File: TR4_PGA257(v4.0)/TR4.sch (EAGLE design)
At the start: 159 parts, among them IC1 SN74AVC4T774PWR, IC2 W25Q256JVFIQ, IC3 SN74AVC4T774PWR, IC4 SN74AVC4T774PWR, IC6 CP2102-GMR, IC7 LM1117MP-1.8_NOPB, IC8 LM1117MP-1.8_NOPB, IC9 LM1117MP-1.8_NOPB, J1 U-F-M5DD-Y-L, J3 TF-15X15, J4 2985-6004, J5 2985-6004, Q1 FMMT497TA, Q10 BSH103,235, Q11 BSH103,235, Q12 BSH103,235, Q13 BSH103,235, Q2 FMMT497TA, Q3 BSH103,235, Q4 BSH103,235, Q5 BSH103,235, Q6 BSH103,235, Q7 BSH103,235, Q8 BSH103,235, Q9 BSH103,235

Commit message: Add pull resistor for mosfet
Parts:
- added R61, R62, R63, R64, R65, R66, R67, R68, R69, R70, R71: 10k, SparkFun-Resistors:10KOHM-0603-1/10W-1%
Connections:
- net GND: now also R61.1, R62.1, R63.1, R64.1, R65.1, R66.1, R67.1, R68.1, R69.1, R70.1, R71.1
- net LED_0: now also R64.2
- net LED_1: now also R65.2
- net LED_2: now also R66.2
- net LED_3: now also R67.2
- net LED_4: now also R68.2
- net LED_5: now also R69.2
- net LED_6: now also R70.2
- net LED_7: now also R71.2
- net VDD_1.8_1: now also R63.2
- net VDD_1.8_2: now also R61.2
- net VDD_1.8_3: now also R62.2

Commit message: Update signal name and connect pin 59 and 60
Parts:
- removed C1, C10, C11, C6: 0.1uF, SparkFun-Capacitors:0.1UF-0603-25V-5%
- removed C12: 4.7uF, SparkFun-Capacitors:4.7UF0603
- removed C9: 1.0uF, SparkFun-Capacitors:1.0UF-0603-16V-10%
- removed CHILDCLOCK, CLOCK: (no value), pinhead:PINHD-2X2
- removed D1, D2, D3: (no value), SparkFun-LED:LED0603
- removed IC2: W25Q256JVFIQ, SamacSys_Parts:W25Q256JVFIQ
- removed IC6: CP2102-GMR, SamacSys_Parts:CP2102-GMR
- removed J1: U-F-M5DD-Y-L, SamacSys_Parts:U-F-M5DD-Y-L
- removed J2: (no value), SparkFun-Connectors:CONN_07
- removed J3: TF-15X15, SamacSys_Parts:TF-15X15
- removed JP7: PINHD-2X2, Connector:PINHD-2X2
- removed Q1, Q2: FMMT497TA, SamacSys_Parts:FMMT497TA
- removed R11, R12, R13: 10k, SparkFun-Resistors:10KOHM-0603-1/10W-1%
- removed R14, R15, R16, R18, R19, R20, R21: 33, SparkFun-Resistors:33OHM-0603-1/10W-1%
- removed R34, R35, R36, R40, R41, R43, R44: 4.7k, SparkFun-Resistors:4.7KOHM-0603-1/10W-1%
- removed R37, R38, R39: 330, SparkFun-Resistors:330OHM-0603-1/10W-1%
- removed R42, R45: 47k, SparkFun-Resistors:47KOHM-0603-1/10W-1%
- removed R7, R8: 20k, SparkFun-Resistors:20KOHM-0603-1/10W-1%
- added FLASH, SD_CARD: PINHD-2X6, Connector:PINHD-2X6
- added USB-UART: PINHD-2X4, Connector:PINHD-2X4
- C14, C16, C18: value 10uF -> 100uF
- IC7, IC8, IC9: value LM1117MP-1.8_NOPB -> LM1117IMPX-ADJ/NOPB
- R1: value 200 -> 15k; device SparkFun-Resistors:200OHM-0603-1/10W-1% -> SparkFun-Resistors:15KOHM-0603-1/10W-1%
- R2, R4, R6: value 20k -> 6.8k; device SparkFun-Resistors:20KOHM-0603-1/10W-1% -> SparkFun-Resistors:6.8KOHM-0603-1/10W-1%
- R3, R5: value 20k -> 15k; device SparkFun-Resistors:20KOHM-0603-1/10W-1% -> SparkFun-Resistors:15KOHM-0603-1/10W-1%
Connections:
- net VDD_CORE renamed VDD_CHIP
- net VDD_IO_CORE renamed VDD_CHIP_IO
- removed net CD1: R1.2, R8.1
- removed net D+: IC6.D+, J1.3
- removed net D-: IC6.D-, J1.2
- removed net DAT1: J3.DAT1
- removed net DAT2: J3.DAT2, R7.1
- removed net FLASH_HOLD: IC2.!RESET(IO3), R12.1, R18.1
- removed net FLASH_RESET: IC2.!RESET, R13.1, R16.1
- removed net FLASH_WP: IC2.!WP(IO2), R11.1, R21.1
- removed net N$1: J2.4, R14.2
- removed net N$11: J2.7, R21.2
- removed net N$2: J2.5, R19.2
- removed net N$25: IC6.!RST, R34.2
- removed net N$27: IC6.!SUSPEND, R35.2
- removed net N$29: IC6.SUSPEND, R36.2
- removed net N$3: J3.CARD_DETECT, R1.1
- removed net N$30: JP7.2, Q1.C, R40.1
- removed net N$31: Q1.B, R41.1
- removed net N$32: D1.A, R37.1
- removed net N$33: D2.A, R38.1
- removed net N$34: D3.A, R39.1
- removed net N$35: JP7.4, Q2.E, R44.2
- removed net N$36: R43.1, R44.1
- removed net N$37: Q2.B, R43.2
- removed net N$5: J2.3, R15.2
- removed net N$6: J2.6, R20.2
- removed net N$7: J2.1, R18.2
- removed net N$8: J2.2, R16.2
- removed net RXD: D3.C, IC6.RXD, Q2.C, R45.2
- removed net SMA_ICHILD: CHILDCLOCK.1, J5.5
- removed net SMA_ICLK: CLOCK.1, J4.5
- removed net TXD: D2.C, IC6.TXD, Q1.E, R42.1
- removed net VDD_5V: C10.1, C9.1, IC6.REGIN, IC6.VBUS, J1.1, R34.1, R35.1, R37.2
- removed net VDD_CP2102: C11.1, C12.1, IC6.VDD, R38.2, R39.2, R42.2, R45.1
- removed net VDD_IO: C3.1, C5.1, C8.1, IC1.DIR1, IC1.DIR2, IC1.DIR3, IC1.VCCA, IC3.DIR1, IC3.DIR2, IC3.DIR4, IC3.VCCA, IC4.DIR4, IC4.VCCA, JP8.2, R26.2, R27.2, R28.2, R29.2, R30.2, R31.2, R32.2, R33.2, R40.2, R41.2, R58.2, R59.2, R60.2
- new net VDD_1V8: C3.1, C5.1, C8.1, IC1.DIR1, IC1.DIR2, IC1.DIR3, IC1.VCCA, IC3.DIR1, IC3.DIR3, IC3.DIR4, IC3.VCCA, IC4.DIR4, IC4.VCCA, JP8.2, R26.2, R27.2, R28.2, R29.2, R30.2, R31.2, R32.2, R33.2, R58.2, R59.2, R60.2, USB-UART.5
- net B1: now also SD_CARD.12; no longer J3.CD/DAT3, R2.1
- net B2: now also SD_CARD.10; no longer J3.CMD, R3.1
- net B3: now also SD_CARD.6; no longer J3.CLX, R4.1
- net B4: now also SD_CARD.8; no longer J3.DAT0, R5.1
- net CHILDCLOCK: now also J5.5; no longer CHILDCLOCK.2, CHILDCLOCK.4
- net CHILDCLOCK_GPIO: no longer CHILDCLOCK.3
- net CLOCK_GPIO: no longer CLOCK.3
- net CS: now also IC3.A1, JP2.2; no longer IC3.A4, JP2.8
- net DAT0: no longer R6.1
- net FLASH_CS: now also FLASH.12, IC3.B1; no longer IC2.DO(IO1), IC3.B4, R15.1
- net FLASH_MISO: now also FLASH.8, IC3.B2; no longer IC2.!CS, IC3.B3, R14.1
- net FLASH_MOSI: now also FLASH.10, IC3.B3; no longer IC2.DI(IO0), IC3.B2, R19.1
- net FLASH_SCK: now also FLASH.6, IC3.B4; no longer IC2.CLK, IC3.B1, R20.1
- net GND: now also FLASH.3, FLASH.4, IC3.DIR2, R1.1, R2.1, R2.2, R3.1, R4.1, R4.2, R5.1, R6.1, R6.2, SD_CARD.3, SD_CARD.4, USB-UART.1; no longer C1.2, C10.2, C11.2, C12.2, C6.2, C9.2, D1.C, IC2.GND, IC3.DIR3, IC6.GND, J1.10, J1.5, J1.7, J1.8, J1.9, J3.MP1, J3.MP2, J3.MP3, J3.MP4, J3.VSS, R36.1
- net MISO: now also IC3.A2, JP2.4; no longer IC3.A3, JP2.6
- net MOSI: now also IC3.A3, JP2.6; no longer IC3.A2, JP2.4
- net QSPI_CS: now also JP2.1; no longer JP2.7
- net QSPI_MISO: now also JP2.3; no longer JP2.5
- net QSPI_MOSI: now also JP2.5; no longer JP2.3
- net QSPI_SCK: now also JP2.7; no longer JP2.1
- net SCK: now also IC3.A4, JP2.8; no longer IC3.A1, JP2.2
- net SYS_CLK: now also J4.5; no longer CLOCK.2, CLOCK.4
- net TLPORT_A_BITS_PARAM[0]: now also SOCKET_2.28
- net UART_RXD: now also USB-UART.3; no longer JP7.1
- net UART_TXD: now also USB-UART.7; no longer JP7.3
- net VDD_1.8_1: now also R1.2
- net VDD_1.8_2: now also R3.2
- net VDD_1.8_3: now also R5.2
- net VDD_3V3: now also FLASH.1, FLASH.2, SD_CARD.1, SD_CARD.2; no longer C1.1, C6.1, IC2.VCC, J3.VDD, R11.2, R12.2, R13.2, R2.2, R3.2, R4.2, R5.2, R6.2, R7.2, R8.2
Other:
- moved on the sheet: C13, C15, C17, D4, IC7, R1, R2, R3, R4, R46, R5, R6

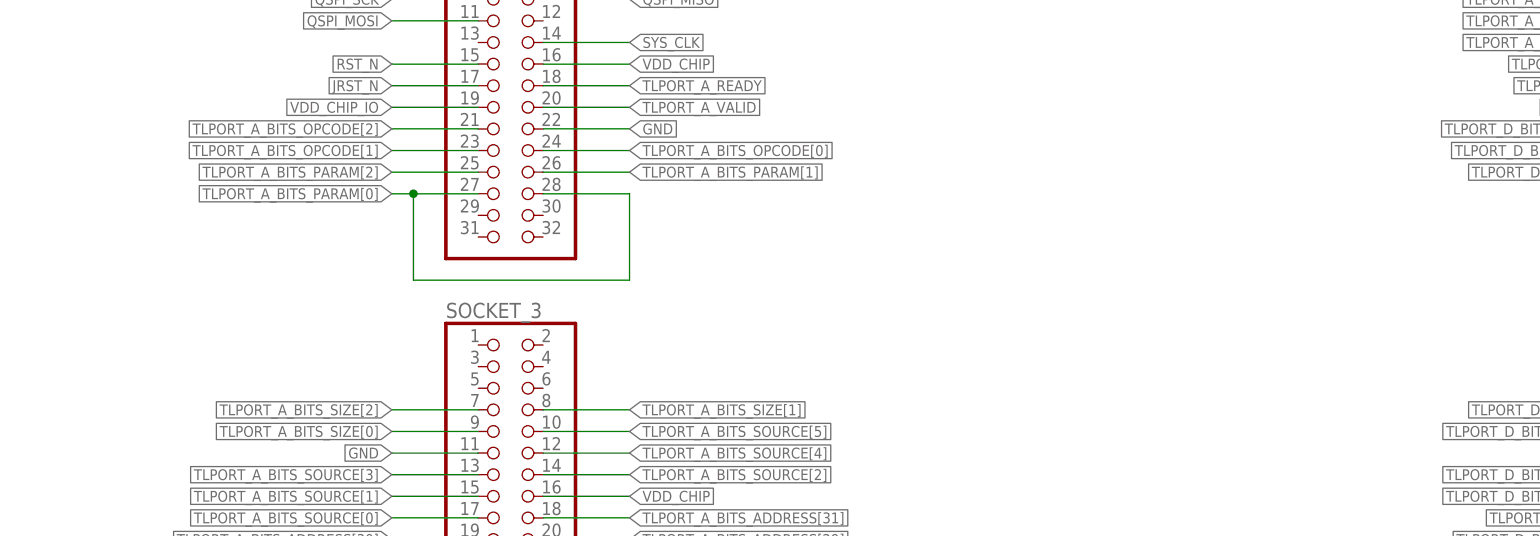
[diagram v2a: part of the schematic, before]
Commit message: put header for param[0] signal
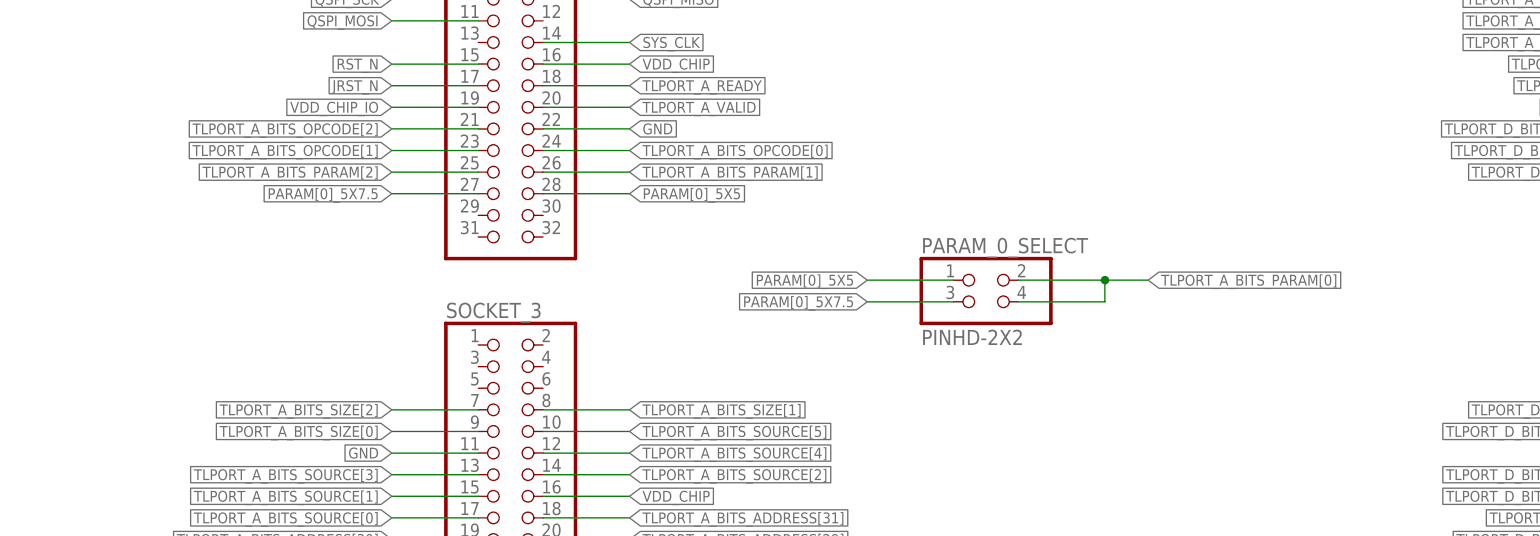
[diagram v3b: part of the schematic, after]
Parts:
- added PARAM_0_SELECT: PINHD-2X2, Connector:PINHD-2X2
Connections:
- new net PARAM[0]_5X5: PARAM_0_SELECT.1, SOCKET_2.28
- new net PARAM[0]_5X7.5: PARAM_0_SELECT.3, SOCKET_2.27
- net TLPORT_A_BITS_PARAM[0]: now also PARAM_0_SELECT.2, PARAM_0_SELECT.4; no longer SOCKET_2.27, SOCKET_2.28
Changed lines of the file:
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@@
 <part name="R5" library="SparkFun-Resistors" library_urn="urn:adsk.eagle:library:532" deviceset="15KOHM" device="-0603-1/10W-1%" package3d_urn="urn:adsk.eagle:package:39650/1" value="15k"/>
 <part name="R6" library="SparkFun-Resistors" library_urn="urn:adsk.eagle:library:532" deviceset="6.8KOHM" device="-0603-1/10W-1%" package3d_urn="urn:adsk.eagle:package:39650/1" value="6.8k"/>
+<part name="PARAM_0_SELECT" library="Connector" library_urn="urn:adsk.eagle:library:16378166" deviceset="PINHD-2X2" device="" package3d_urn="urn:adsk.eagle:package:22455/2"/>
 </parts>
 <sheets>
@@
 <attribute name="VALUE" x="-63.5" y="-390.144" size="1.778" layer="96" font="vector" align="top-center"/>
 </instance>
+<instance part="PARAM_0_SELECT" gate="A" x="548.64" y="-228.6" smashed="yes">
+<attribute name="NAME" x="539.75" y="-222.885" size="1.778" layer="95"/>
+<attribute name="VALUE" x="539.75" y="-233.68" size="1.778" layer="96"/>
+</instance>
 </instances>
 <busses>
@@
 <net name="TLPORT_A_BITS_PARAM[0]" class="0">
 <segment>
-<pinref part="SOCKET_2" gate="A" pin="27"/>
-<wire x1="487.68" y1="-215.9" x2="480.06" y2="-215.9" width="0.1524" layer="91"/>
-<label x="477.52" y="-215.9" size="1.27" layer="95" rot="R180" xref="yes"/>
-<pinref part="SOCKET_2" gate="A" pin="28"/>
-<wire x1="480.06" y1="-215.9" x2="477.52" y2="-215.9" width="0.1524" layer="91"/>
-<wire x1="495.3" y1="-215.9" x2="505.46" y2="-215.9" width="0.1524" layer="91"/>
-<wire x1="505.46" y1="-215.9" x2="505.46" y2="-226.06" width="0.1524" layer="91"/>
-<wire x1="505.46" y1="-226.06" x2="480.06" y2="-226.06" width="0.1524" layer="91"/>
-<wire x1="480.06" y1="-226.06" x2="480.06" y2="-215.9" width="0.1524" layer="91"/>
-<junction x="480.06" y="-215.9"/>
-</segment>
-<segment>
 <pinref part="JP18" gate="A" pin="13"/>
 <wire x1="492.76" y1="78.74" x2="482.6" y2="78.74" width="0.1524" layer="91"/>
 <label x="482.6" y="78.74" size="1.27" layer="95" rot="R180" xref="yes"/>
 </segment>
+<segment>
+<pinref part="PARAM_0_SELECT" gate="A" pin="4"/>
+<wire x1="551.18" y1="-228.6" x2="561.34" y2="-228.6" width="0.1524" layer="91"/>
+<pinref part="PARAM_0_SELECT" gate="A" pin="2"/>
+<wire x1="551.18" y1="-226.06" x2="561.34" y2="-226.06" width="0.1524" layer="91"/>
+<wire x1="561.34" y1="-228.6" x2="561.34" y2="-226.06" width="0.1524" layer="91"/>
+<wire x1="561.34" y1="-226.06" x2="566.42" y2="-226.06" width="0.1524" layer="91"/>
+<junction x="561.34" y="-226.06"/>
+<label x="566.42" y="-226.06" size="1.27" layer="95" xref="yes"/>
+</segment>
 </net>
 <net name="N$249" class="0">
@@
 </segment>
 </net>
+<net name="PARAM[0]_5X7.5" class="0">
+<segment>
+<pinref part="SOCKET_2" gate="A" pin="27"/>
+<wire x1="487.68" y1="-215.9" x2="477.52" y2="-215.9" width="0.1524" layer="91"/>
+<label x="477.52" y="-215.9" size="1.27" layer="95" rot="R180" xref="yes"/>
+</segment>
+<segment>
+<pinref part="PARAM_0_SELECT" gate="A" pin="3"/>
+<wire x1="543.56" y1="-228.6" x2="533.4" y2="-228.6" width="0.1524" layer="91"/>
+<label x="533.4" y="-228.6" size="1.27" layer="95" rot="R180" xref="yes"/>
+</segment>
+</net>
+<net name="PARAM[0]_5X5" class="0">
+<segment>
+<pinref part="SOCKET_2" gate="A" pin="28"/>
+<wire x1="495.3" y1="-215.9" x2="505.46" y2="-215.9" width="0.1524" layer="91"/>
+<label x="505.46" y="-215.9" size="1.27" layer="95" xref="yes"/>
+</segment>
+<segment>
+<pinref part="PARAM_0_SELECT" gate="A" pin="1"/>
+<wire x1="543.56" y1="-226.06" x2="533.4" y2="-226.06" width="0.1524" layer="91"/>
+<label x="533.4" y="-226.06" size="1.27" layer="95" rot="R180" xref="yes"/>
+</segment>
+</net>

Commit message: update file
update BOM, position, and Gerber file, change the footprint of the level shifter
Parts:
- removed C7, C8: 0.1uF, SparkFun-Capacitors:0.1UF-0603-25V-5%
- removed IC4: SN74AVC4T774PWR, SamacSys_Parts:SN74AVC4T774PWR
- removed R10, R17: 10k, SparkFun-Resistors:10KOHM-0603-1/10W-1%
- added C1, C6: 0.1uF, SparkFun-Capacitors:0.1UF-0603-25V-5%
- added IC2: SN74AVC4T774RSVR, SamacSys_Parts:SN74AVC4T774RSVR
- added R7, R8: 10k, SparkFun-Resistors:10KOHM-0603-1/10W-1%
- IC1, IC3: value SN74AVC4T774PWR -> SN74AVC4T774RSVR; device SamacSys_Parts:SN74AVC4T774PWR -> SamacSys_Parts:SN74AVC4T774RSVR
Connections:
- removed net CLK: IC1.A3, JP1.6
- removed net CMD: IC1.A2, JP1.4
- removed net CS: IC3.A1, JP2.2
- removed net DAT0: IC1.A4, JP1.8
- removed net DAT3: IC1.A1, JP1.2
- removed net MISO: IC3.A2, JP2.4
- removed net MOSI: IC3.A3, JP2.6
- removed net N$16: IC4.!OE, R17.2
- removed net SCK: IC3.A4, JP2.8
- new net N$1: IC2.!OE, R7.2
- new net N$11: IC1.A1, JP2.2
- new net N$2: IC2.A1, JP1.2
- new net N$25: IC3.!OE, R9.2
- new net N$3: IC2.A2, JP1.4
- new net N$5: IC2.A3, JP1.6
- new net N$6: IC2.A4, JP1.8
- new net N$7: IC1.!OE, R8.2
- new net N$8: IC1.A4, JP2.8
- net B1: now also IC2.B1; no longer IC1.B1
- net B2: now also IC2.B2; no longer IC1.B2
- net B3: now also IC2.B3; no longer IC1.B3
- net B4: now also IC2.B4; no longer IC1.B4
- net FLASH_CS: now also IC1.B1; no longer IC3.B1
- net FLASH_MISO: now also IC1.B2; no longer IC3.B2
- net FLASH_MOSI: now also IC1.B3; no longer IC3.B3
- net FLASH_SCK: now also IC1.B4; no longer IC3.B4
- net GND: now also C1.2, C6.2, IC1.DIR2, IC2.DIR4, IC2.GND, IC3.DIR1, IC3.DIR3, R7.1, R8.1; no longer C7.2, C8.2, IC1.DIR4, IC4.DIR1, IC4.DIR2, IC4.DIR3, IC4.GND, R10.1, R17.1
- net N$10: now also IC1.A2, JP2.4; no longer IC3.!OE, R10.2
- net N$12: now also IC3.A1; no longer IC4.A1
- net N$13: now also IC3.A2; no longer IC4.A2
- net N$14: now also IC3.A3; no longer IC4.A3
- net N$15: now also IC3.A4; no longer IC4.A4
- net N$9: now also IC1.A3, JP2.6; no longer IC1.!OE, R9.2
- net TCK: now also IC3.B3; no longer IC4.B3
- net TDI: now also IC3.B1; no longer IC4.B1
- net TDO: now also IC3.B4; no longer IC4.B4
- net TMS: now also IC3.B2; no longer IC4.B2
- net VDD_1V8: now also C6.1, IC1.DIR4, IC2.DIR1, IC2.DIR2, IC2.DIR3, IC2.VCCA; no longer C8.1, IC1.DIR2, IC3.DIR1, IC3.DIR3, IC4.DIR4, IC4.VCCA
- net VDD_3V3: now also C1.1, IC2.VCCB; no longer C7.1, IC4.VCCB
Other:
- moved on the sheet: C2, C3, C4, C5, FLASH, IC1, IC3, JTAG_20_PIN, R22, R23, R24, R25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
